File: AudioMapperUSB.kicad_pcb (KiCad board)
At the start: 2 copper layers, 100 x 100 mm, 98 parts, among them J1 USB_B, J10 Conn_01x01, J11 Conn_01x01, J2 Audio-Jack-2, J3 Conn_01x02, J4 Audio-Jack-2, J5 Conn_01x02, J6 Conn_01x02, J7 Conn_01x02, J8 Conn_01x01, J9 Conn_01x01, Q1 SS8550, U1 AMS1117-3.3, U2 PCM2900, U3 OPA2170, U4 OPA2170, U5 OPA2170, Y1 12 MHz

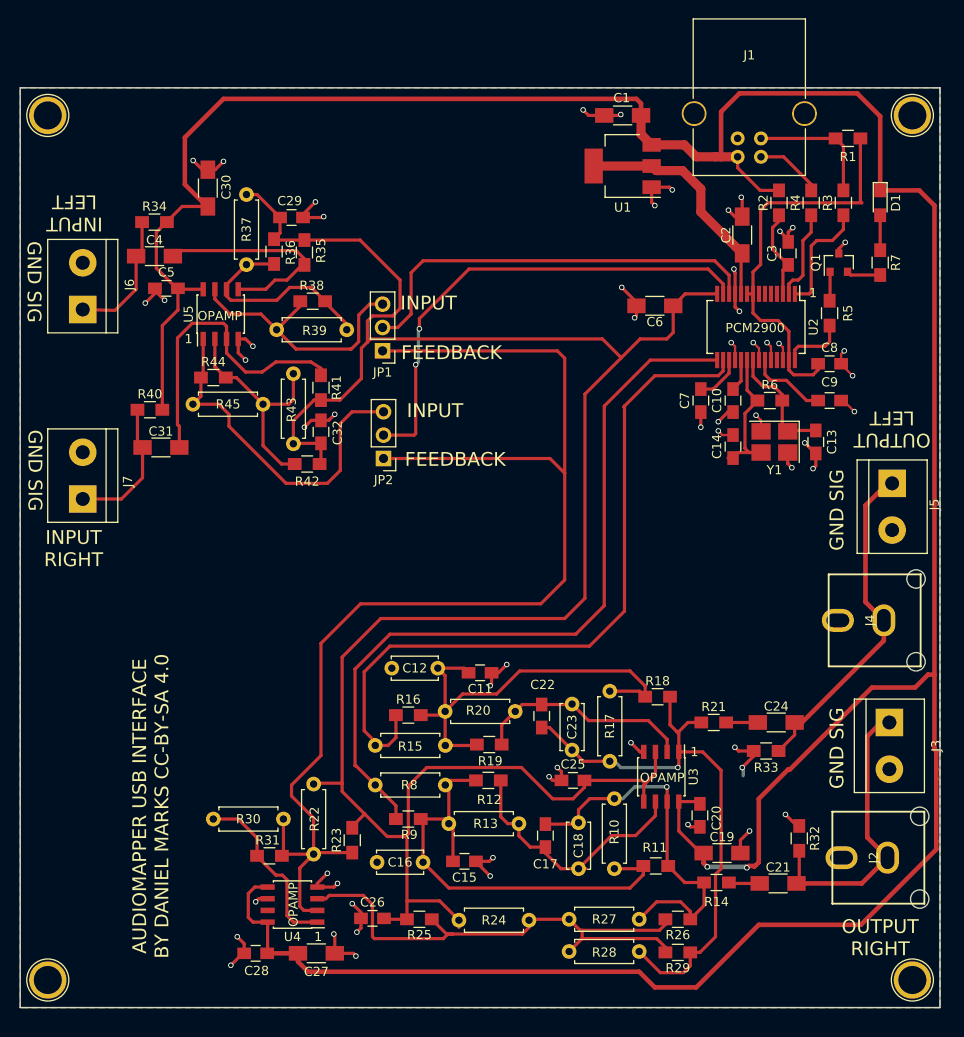
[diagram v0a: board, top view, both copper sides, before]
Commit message: Added second gain stage to microphone
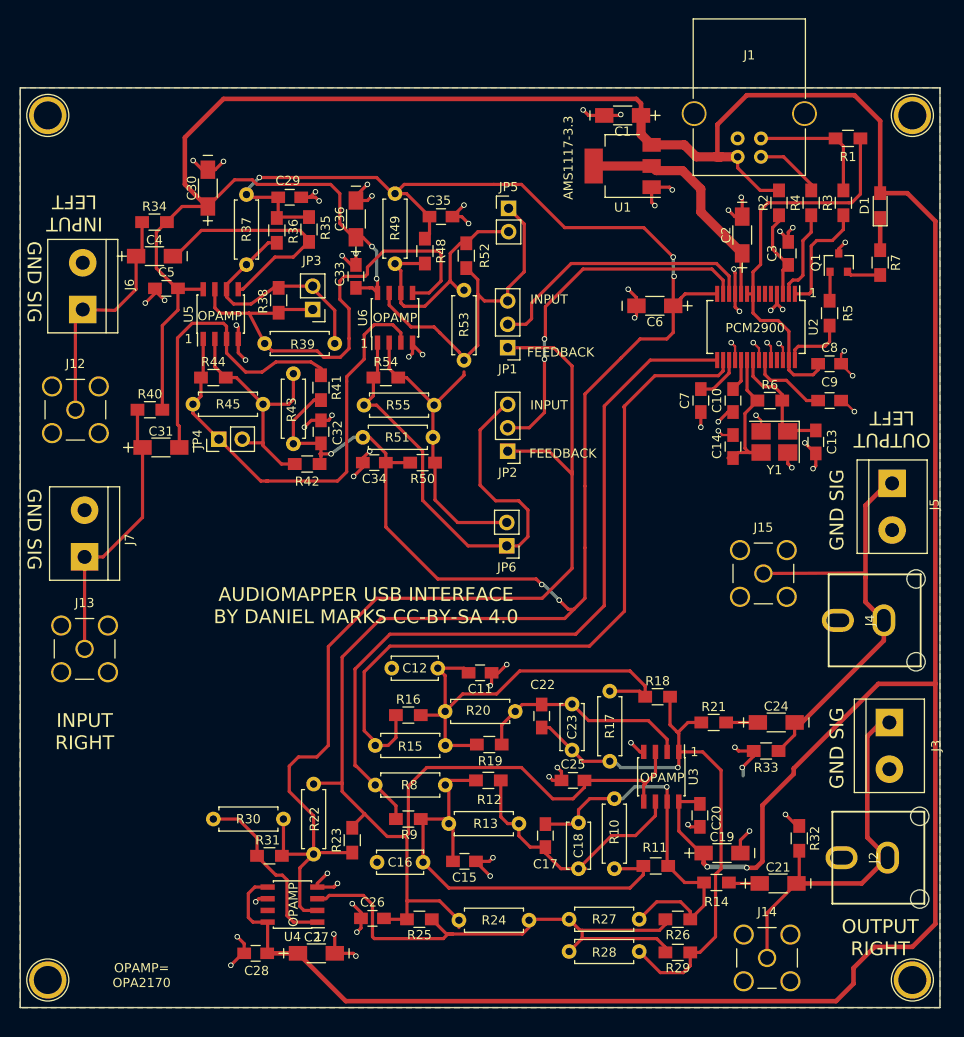
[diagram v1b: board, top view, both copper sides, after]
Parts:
- added C33: 1 uF, Capacitors_SMD:C_0805_HandSoldering, F.Cu at (66.5, 50.5)
- added C34: 1 uF, Capacitors_SMD:C_0805_HandSoldering, F.Cu at (68.5, 70.8)
- added C35: 1 uF, Capacitors_SMD:C_0805_HandSoldering, F.Cu at (75.8, 44.0)
- added C36: 10 uF, AudioMapperUSB:CP_1206_HandSoldering, F.Cu at (66.5, 44.2)
- added J12: Conn_Coaxial, Connectors:SMA_THT_Jack_Straight, F.Cu at (36.0, 65.0)
- added J13: Conn_Coaxial, Connectors:SMA_THT_Jack_Straight, F.Cu at (37.0, 91.0)
- added J14: Conn_Coaxial, Connectors:SMA_THT_Jack_Straight, F.Cu at (111.2, 124.6)
- added J15: Conn_Coaxial, Connectors:SMA_THT_Jack_Straight, F.Cu at (110.8, 82.8)
- added JP3: Jumper_NO_Small, Pin_Headers:Pin_Header_Straight_1x02_Pitch2.54mm, F.Cu at (61.8, 54.1)
- added JP4: Jumper_NO_Small, Pin_Headers:Pin_Header_Straight_1x02_Pitch2.54mm, F.Cu at (51.6, 68.2)
- added JP5: Jumper_NO_Small, Pin_Headers:Pin_Header_Straight_1x02_Pitch2.54mm, F.Cu at (83.1, 43.1)
- added JP6: Jumper_NO_Small, Pin_Headers:Pin_Header_Straight_1x02_Pitch2.54mm, F.Cu at (82.9, 79.8)
- added R48: 10k, Resistors_SMD:R_0805_HandSoldering, F.Cu at (74.0, 47.8)
- added R49: NO, Resistors_THT:R_Axial_DIN0207_L6.3mm_D2.5mm_P7.62mm_Horizontal, F.Cu at (70.8, 41.5)
- added R50: 10k, Resistors_SMD:R_0805_HandSoldering, F.Cu at (73.8, 70.8)
- added R51: NO, Resistors_THT:R_Axial_DIN0207_L6.3mm_D2.5mm_P7.62mm_Horizontal, F.Cu at (67.2, 68.0)
- added R52: 100k, Resistors_SMD:R_0805_HandSoldering, F.Cu at (78.5, 48.2)
- added R53: NO, Resistors_THT:R_Axial_DIN0207_L6.3mm_D2.5mm_P7.62mm_Horizontal, F.Cu at (78.2, 52.0)
- added R54: 100k, Resistors_SMD:R_0805_HandSoldering, F.Cu at (69.8, 61.5)
- added R55: NO, Resistors_THT:R_Axial_DIN0207_L6.3mm_D2.5mm_P7.62mm_Horizontal, F.Cu at (75.0, 64.5)
- added U6: OPA2170, Housings_SOIC:SOIC-8_3.9x4.9mm_Pitch1.27mm, F.Cu at (70.8, 55.0)
- C1, C19, C2, C21, C24, C27, C30, C31, C4, C6: footprint Capacitors_SMD:C_1206_HandSoldering -> AudioMapperUSB:CP_1206_HandSoldering
- moved JP1 13.6 mm to (83.0, 58.2)
- moved JP2 13.5 mm to (83.0, 69.5)
- moved J7 6.30 mm to (37.0, 81.0)
- moved R38 3.70 mm to (58.1, 53.1), turned to 90 degrees
- moved R35 2.55 mm to (61.4, 45.4)
- moved R36 2.32 mm to (57.9, 45.5)
- moved C29 2.21 mm to (59.3, 41.9)
- moved R39 1.98 mm to (64.2, 57.8)
- moved D1 0.30 mm to (123.5, 42.8), turned to 90 degrees
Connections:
- D1 pad 1: Net-(C1-Pad1) -> Net-(D1-Pad1)
- D1 pad 2: Net-(D1-Pad2) -> Net-(C1-Pad1)
- R38 pad 1: Net-(JP1-Pad3) -> Net-(JP3-Pad1)
- R39 pad 2: Net-(JP1-Pad3) -> Net-(JP3-Pad1)
- R44 pad 1: Net-(JP2-Pad3) -> Net-(JP4-Pad1)
- R45 pad 2: Net-(JP2-Pad3) -> Net-(JP4-Pad1)
- R7 pad 1: Net-(D1-Pad2) -> Net-(D1-Pad1)
- U2 pad 4: (no net) -> GND
- U5 pad 1: Net-(JP2-Pad3) -> Net-(JP4-Pad1)
- U5 pad 7: Net-(JP1-Pad3) -> Net-(JP3-Pad1)
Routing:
- net Net-(JP3-Pad1): track 0.00 -> 54.7 mm
- net Net-(JP4-Pad1): track 0.00 -> 50.8 mm
- net VCOM: track 242.7 -> 289.9 mm, vias 0 -> 6
- net Net-(C1-Pad1): track 362.3 -> 399.3 mm, vias 2 -> 4
- net Net-(JP6-Pad2): track 0.00 -> 33.6 mm
- net Net-(JP5-Pad2): track 0.00 -> 26.7 mm
- net Net-(JP1-Pad1): track 139.4 -> 115.0 mm
- net GND: track 116.3 -> 137.4 mm, vias 58 -> 70
- net VINL: track 46.0 -> 30.3 mm
- net Net-(JP2-Pad3): track 38.8 -> 54.5 mm
- net Net-(C31-Pad1): track 15.3 -> 30.2 mm
- net VINR: track 53.2 -> 39.2 mm
- net Net-(C24-Pad2): track 36.6 -> 48.4 mm
- net Net-(C4-Pad1): track 14.3 -> 25.6 mm
- net Net-(C21-Pad2): track 31.9 -> 41.9 mm
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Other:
- board text added: "AMS1117-3.3"
- board text added: "OPAMP= OPA2170"

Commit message: Added antialiasing on input and SP/DIF input/output
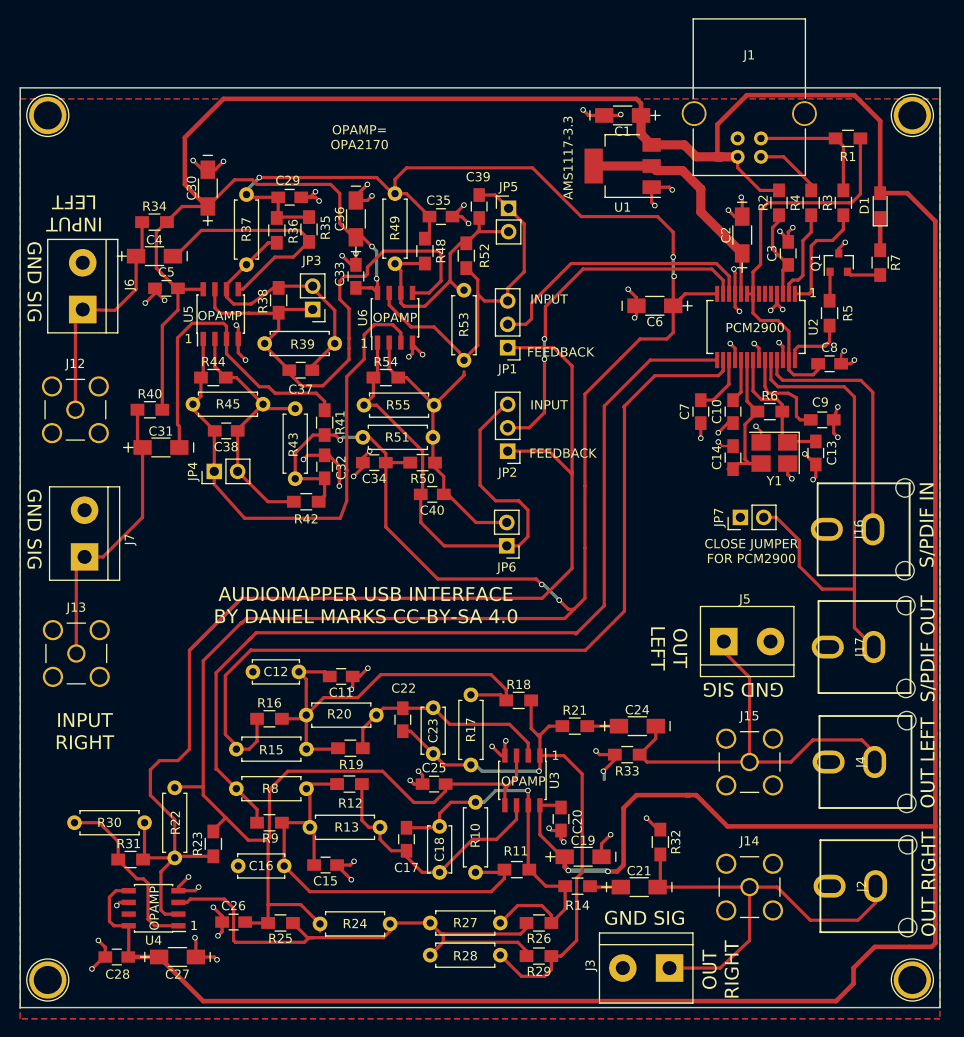
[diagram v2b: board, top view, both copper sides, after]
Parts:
- added C37: 22 pF, Capacitors_SMD:C_0805_HandSoldering, F.Cu at (60.5, 60.7)
- added C38: 22 pF, Capacitors_SMD:C_0805_HandSoldering, F.Cu at (52.4, 67.3)
- added C39: 22 pF, Capacitors_SMD:C_0805_HandSoldering, F.Cu at (79.9, 42.9)
- added C40: 22 pF, Capacitors_SMD:C_0805_HandSoldering, F.Cu at (74.8, 74.2)
- added J16: Audio-Jack-2, AudioMapperUSB:RCAConnectorCommon, F.Cu at (121.7, 78.0)
- added J17: Audio-Jack-2, AudioMapperUSB:RCAConnectorCommon, F.Cu at (121.8, 90.8)
- added JP7: Jumper_NC_Small, Pin_Headers:Pin_Header_Straight_1x02_Pitch2.54mm, F.Cu at (108.3, 76.7)
- R11, R18: value 3K9 -> 12K
- R12, R19: value 12K -> 3k9
- R36, R42, R48, R50: value 10k -> 4k7
- moved J3 35.8 mm to (100.6, 125.7), turned to 180 degrees
- moved J5 25.1 mm to (106.5, 90.2), turned to 0 degrees
- moved J15 20.6 mm to (109.3, 103.3)
- moved J4 15.4 mm to (121.9, 103.3)
- moved C12 15.1 mm to (55.3, 93.5)
- moved C18 15.1 mm to (75.6, 115.3)
- moved C20 15.1 mm to (88.8, 109.5)
- moved C21 15.1 mm to (97.3, 116.9)
- moved C22 15.1 mm to (71.6, 98.7)
- moved C24 15.1 mm to (97.1, 99.4)
- moved R12 15.1 mm to (65.8, 105.7)
- moved R14 15.1 mm to (90.6, 116.8)
- moved R21 15.1 mm to (90.3, 99.4)
- moved R25 15.1 mm to (58.3, 120.8)
- moved R32 15.1 mm to (99.6, 112.0)
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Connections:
- C9 pad 1: GND -> Net-(C9-Pad1)
- C9 pad 2: Net-(C9-Pad2) -> GND
- U2 pad 23: Net-(C9-Pad2) -> Net-(C9-Pad1)
- U2 pad 24: GND -> Net-(J17-Pad1)
- U2 pad 25: (no net) -> Net-(J16-Pad1)
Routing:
- net Net-(J17-Pad1): track 0.00 -> 54.8 mm
- net Net-(C1-Pad1): track 399.3 -> 427.2 mm
- net Net-(J16-Pad1): track 0.00 -> 27.7 mm
- net Net-(JP1-Pad1): track 115.0 -> 137.7 mm
- net VCOM: track 289.9 -> 311.0 mm
- net VOUTR: track 84.2 -> 100.0 mm
- net VOUTL: track 80.5 -> 95.8 mm
- net Net-(C9-Pad1): track 0.00 -> 10.6 mm
- net Net-(C38-Pad2): track 50.8 -> 60.0 mm
- net Net-(C9-Pad2): track 8.52 -> 0.00 mm
- net GND: track 137.4 -> 143.4 mm, vias 70 -> 72
- net Net-(C21-Pad2): track 41.9 -> 47.7 mm
- net Net-(C37-Pad1): track 27.1 -> 31.0 mm
- net Net-(C37-Pad2): track 54.7 -> 58.6 mm
- net Net-(C39-Pad2): track 38.3 -> 42.1 mm
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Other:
- board text added: "CLOSE JUMPER FOR PCM2900"
- board text added: "OUT LEFT"
- board text added: "OUT RIGHT"
- board text added: "S/PDIF IN"
- board text added: "S/PDIF OUT"
- board text removed: "OUTPUT LEFT"
- board text removed: "OUTPUT RIGHT"

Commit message: Added ability to chain outputs of two boards together
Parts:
- added C41: 10 uF, AudioMapperUSB:CP_1206_HandSoldering, F.Cu at (43.0, 128.5)
- added C42: 10 uF, AudioMapperUSB:CP_1206_HandSoldering, F.Cu at (33.3, 117.3)
- added D2: 1N4148WS, Diodes_SMD:D_SOD-323_HandSoldering, F.Cu at (104.5, 46.0)
- added D3: 1N4148WS, Diodes_SMD:D_SOD-323_HandSoldering, F.Cu at (100.1, 47.3)
- added J18: Audio-Jack-2, AudioMapperUSB:RCAConnectorCommon, F.Cu at (37.2, 106.5)
- added J19: Audio-Jack-2, AudioMapperUSB:RCAConnectorCommon, F.Cu at (37.4, 94.3)
- added R46: 1k5, Resistors_SMD:R_0805_HandSoldering, F.Cu at (79.1, 54.2)
- added R47: 1k5, Resistors_SMD:R_0805_HandSoldering, F.Cu at (78.9, 70.1)
- added R56: 1k5, Resistors_SMD:R_0805_HandSoldering, F.Cu at (47.8, 101.5)
- added R57: NO, Resistors_THT:R_Axial_DIN0207_L6.3mm_D2.5mm_P7.62mm_Horizontal, F.Cu at (60.8, 126.3)
- added R58: 4k7, Resistors_SMD:R_0805_HandSoldering, F.Cu at (56.7, 123.5)
- added R59: 100R, Resistors_SMD:R_0805_HandSoldering, F.Cu at (35.5, 120.5)
- added R60: 1M, Resistors_SMD:R_0805_HandSoldering, F.Cu at (45.5, 96.1)
- moved R30 11.2 mm to (38.1, 120.9), turned to 90 degrees
- moved J13 9.41 mm to (35.6, 82.1)
- moved J7 7.71 mm to (36.7, 73.3)
- moved J12 6.60 mm to (35.8, 58.4)
- moved R53 6.00 mm to (78.2, 58.0)
- moved J6 5.50 mm to (36.8, 48.6)
- moved C26 2.18 mm to (52.6, 118.6)
- moved R25 2.12 mm to (58.0, 118.7)
- moved JP7 1.30 mm to (108.4, 75.4)
- moved R31 0.58 mm to (42.3, 113.4), turned to 0 degrees
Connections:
- JP1 pad 3: Net-(C39-Pad2) -> Net-(JP1-Pad3)
- JP2 pad 3: Net-(C40-Pad2) -> Net-(JP2-Pad3)
- R22 pad 2: Net-(JP1-Pad1) -> Net-(R22-Pad2)
- R23 pad 1: Net-(JP1-Pad1) -> Net-(R22-Pad2)
- R30 pad 2: Net-(JP1-Pad1) -> Net-(R22-Pad2)
- R31 pad 1: Net-(JP1-Pad1) -> Net-(R22-Pad2)
- U4 pad 2: Net-(JP1-Pad1) -> Net-(R22-Pad2)
- U4 pad 5: Net-(C1-Pad1) -> Net-(R30-Pad1)
- U4 pad 6: GND -> Net-(R59-Pad1)
- U4 pad 7: (no net) -> Net-(R59-Pad1)
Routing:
- net Net-(C42-Pad2): track 0.00 -> 39.4 mm
- net Net-(R22-Pad2): track 0.00 -> 37.4 mm
- net Net-(JP1-Pad1): track 137.7 -> 100.5 mm
- net Net-(C41-Pad2): track 0.00 -> 33.8 mm, vias 0 -> 2
- net Net-(C41-Pad1): track 0.00 -> 13.4 mm
- net Net-(C39-Pad2): track 42.1 -> 55.4 mm
- net Net-(R59-Pad1): track 0.00 -> 13.0 mm
- net Net-(C2-Pad1): track 26.2 -> 35.1 mm
- net Net-(C31-Pad1): track 31.1 -> 22.8 mm
- net Net-(C40-Pad2): track 57.2 -> 49.2 mm
- net Net-(JP2-Pad3): track 0.00 -> 6.27 mm
- net Net-(C39-Pad1): track 28.2 -> 34.0 mm
- net Net-(C4-Pad1): track 25.6 -> 20.1 mm
- net Net-(C40-Pad1): track 32.7 -> 27.7 mm
- net Net-(JP1-Pad3): track 0.00 -> 4.03 mm
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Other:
- board text added: "CHAIN IN"
- board text added: "CHAIN OUT"

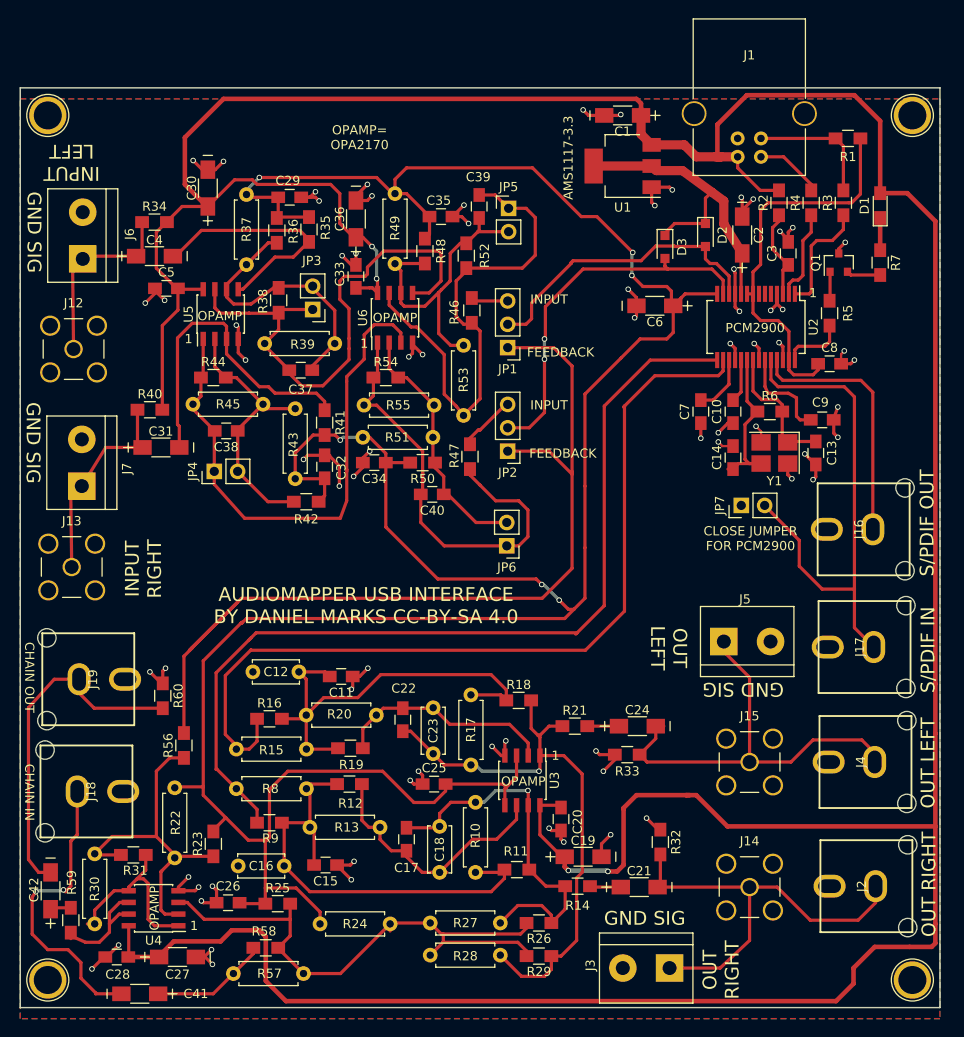
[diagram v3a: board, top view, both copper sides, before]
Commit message: Added real circuit to interface SPDIF levels to 3.3 V CMOS levels
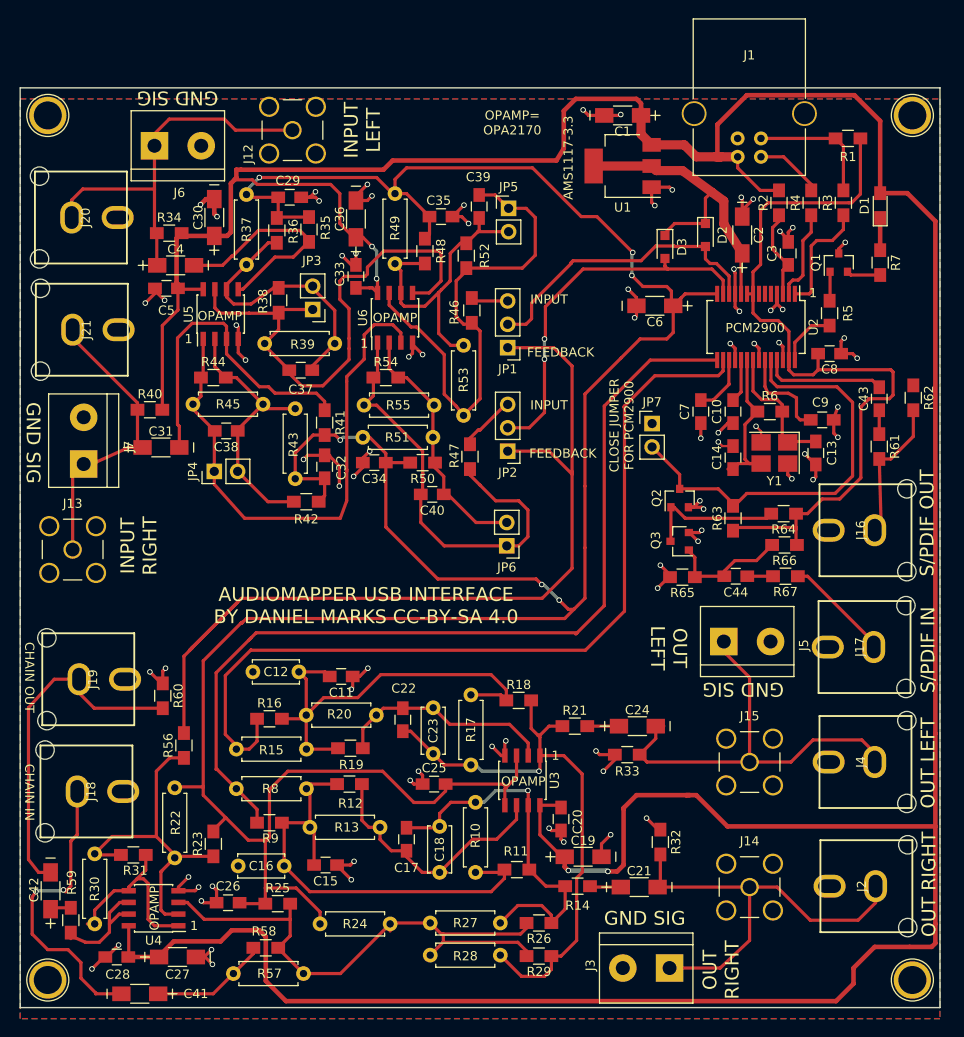
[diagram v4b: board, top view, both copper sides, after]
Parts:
- added C43: 1 uF, Capacitors_SMD:C_0805_HandSoldering, F.Cu at (123.4, 63.8)
- added C44: 1 uF, Capacitors_SMD:C_0805_HandSoldering, F.Cu at (107.8, 83.1)
- added J20: Audio-Jack-2, AudioMapperUSB:RCAConnectorCommon, F.Cu at (36.6, 44.1)
- added J21: Audio-Jack-2, AudioMapperUSB:RCAConnectorCommon, F.Cu at (36.7, 56.3)
- added Q2: MMBT3904, TO_SOT_Packages_SMD:SOT-23, F.Cu at (101.7, 74.6)
- added Q3: MMBT3904, TO_SOT_Packages_SMD:SOT-23, F.Cu at (101.7, 79.3)
- added R61: 220R, Resistors_SMD:R_0805_HandSoldering, F.Cu at (123.4, 69.0)
- added R62: 100R, Resistors_SMD:R_0805_HandSoldering, F.Cu at (127.1, 63.7)
- added R63: 10k, Resistors_SMD:R_0805_HandSoldering, F.Cu at (107.5, 76.8)
- added R64: 10k, Resistors_SMD:R_0805_HandSoldering, F.Cu at (113.0, 76.3)
- added R65: 2k2, Resistors_SMD:R_0805_HandSoldering, F.Cu at (102.0, 83.2)
- added R66: 10k, Resistors_SMD:R_0805_HandSoldering, F.Cu at (113.1, 79.7)
- added R67: 100R, Resistors_SMD:R_0805_HandSoldering, F.Cu at (113.2, 83.1)
- moved J12 33.7 mm to (59.6, 34.6)
- moved J6 14.6 mm to (44.6, 36.3), turned to 0 degrees
- moved JP7 13.2 mm to (98.7, 66.5), turned to 0 degrees
- moved C30 3.28 mm to (51.1, 44.1)
- moved C4 2.51 mm to (46.9, 49.3)
- moved J7 2.41 mm to (36.9, 70.9)
- moved R34 2.00 mm to (46.2, 45.8)
- moved J13 1.90 mm to (35.7, 80.2)
- moved C8 1.10 mm to (118.0, 58.9)
- moved J16 0.22 mm to (121.9, 78.1)
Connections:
- JP7 pad 2: Net-(J17-Pad1) -> Net-(JP7-Pad2)
- U2 pad 24: Net-(J17-Pad1) -> Net-(JP7-Pad2)
- U2 pad 25: Net-(J16-Pad1) -> Net-(C43-Pad2)
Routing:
- net Net-(JP7-Pad2): track 0.00 -> 46.9 mm
- net Net-(J17-Pad1): track 55.2 -> 11.7 mm
- net Net-(C8-Pad1): track 43.5 -> 86.2 mm
- net Net-(C4-Pad1): track 20.1 -> 42.9 mm
- net Net-(Q2-Pad1): track 0.00 -> 15.3 mm
- net Net-(C44-Pad2): track 0.00 -> 13.4 mm
- net Net-(C43-Pad2): track 0.00 -> 13.3 mm
- net Net-(J16-Pad1): track 27.7 -> 15.6 mm
- net GND: track 144.8 -> 154.9 mm, vias 73 -> 79
- net Net-(C31-Pad1): track 22.8 -> 32.7 mm
- net Net-(C1-Pad1): track 425.2 -> 416.8 mm
- net Net-(C44-Pad1): track 0.00 -> 2.80 mm
- net Net-(C43-Pad1): track 0.00 -> 2.60 mm
- net Net-(C4-Pad2): track 28.7 -> 27.2 mm
- net Net-(R5-Pad1): track 7.01 -> 6.46 mm
